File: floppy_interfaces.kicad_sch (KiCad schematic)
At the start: 23 parts, among them J13 Conn_01x04_Male, J14 Conn_02x17_Odd_Even, J16 Conn_01x04_Male, J32 Mini-DIN-8-With-Shield, J6 SDF-60J for IEC 1541 serial p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, U1 74LS374, U2 74LVC374, U22 74LS06N, U3 74LVC374, U4 74LS374

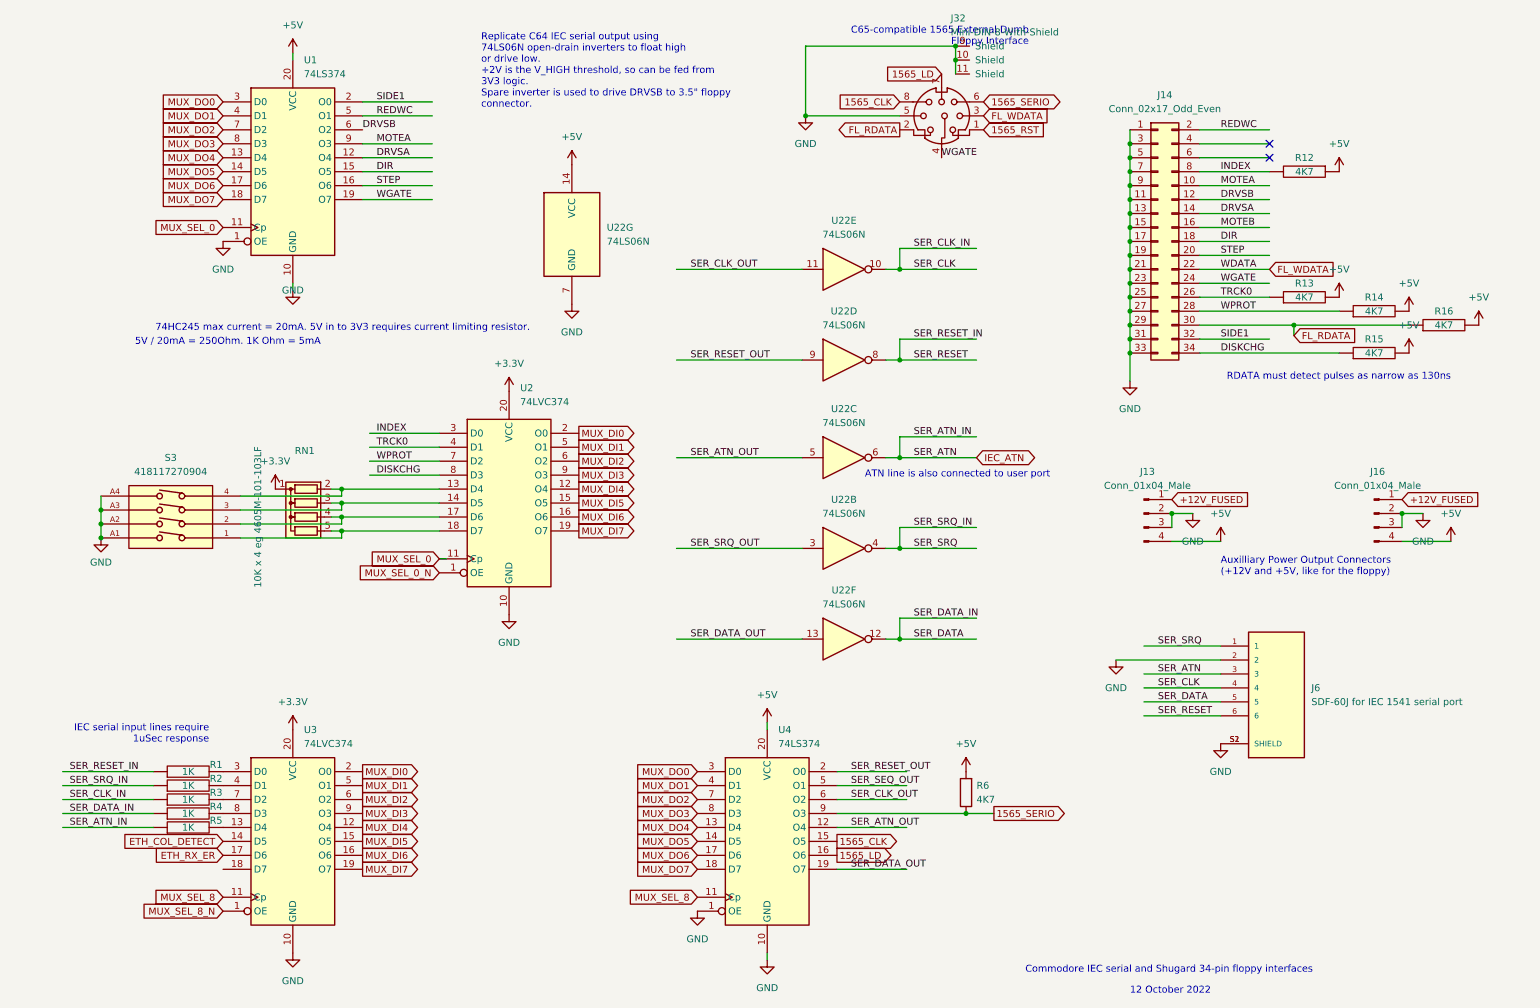
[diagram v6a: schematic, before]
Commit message: rework user port
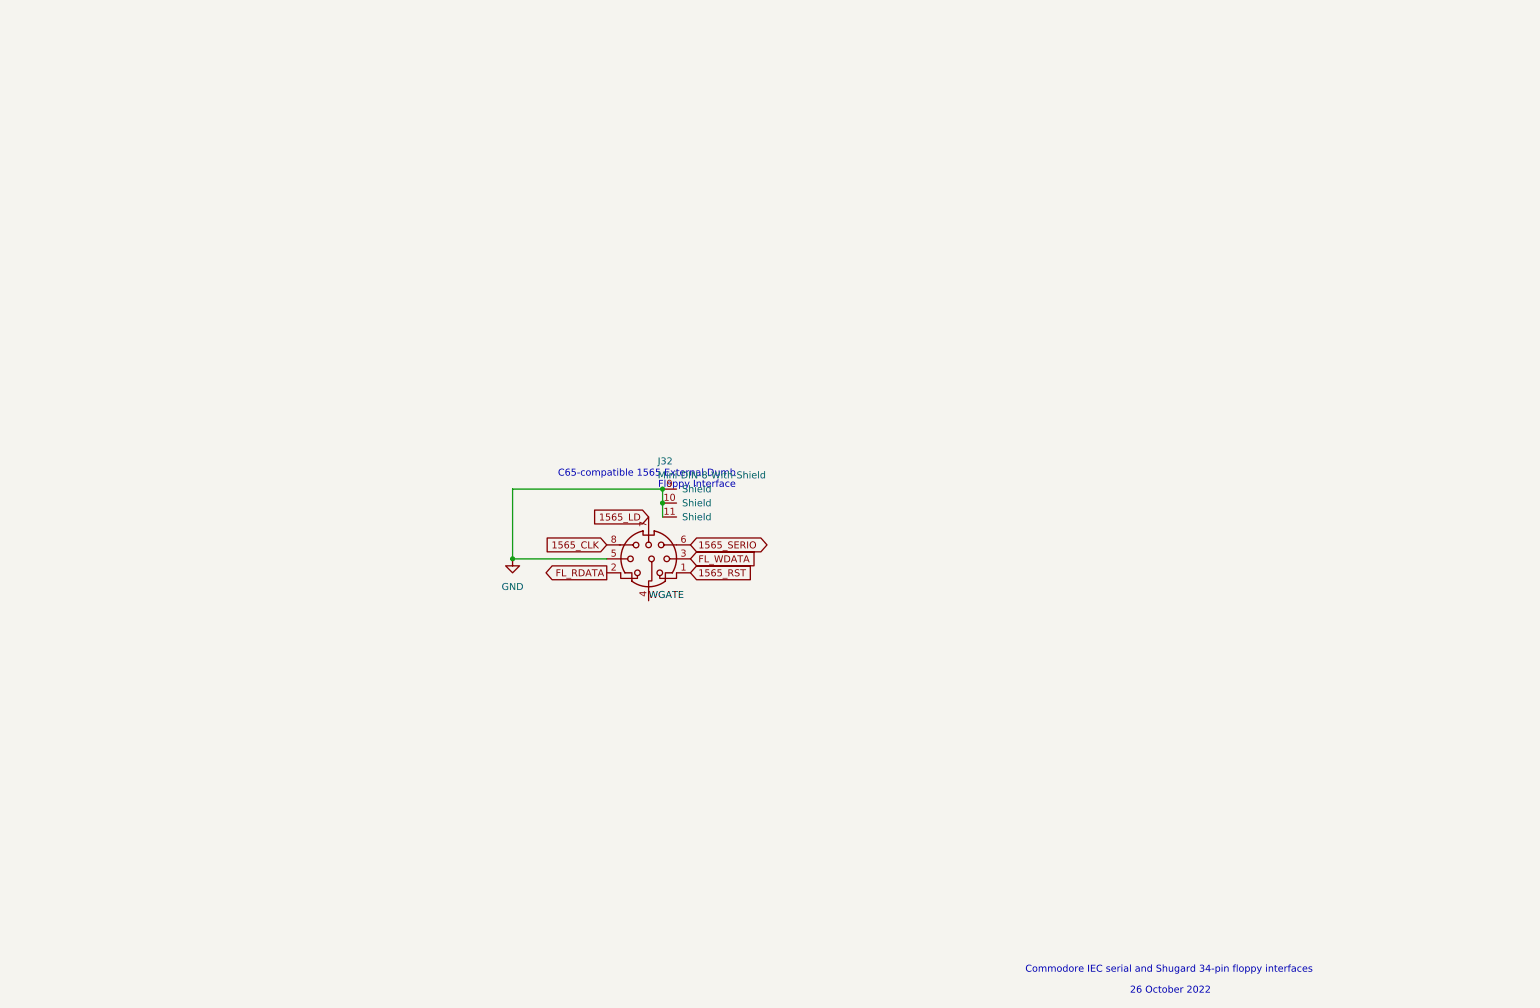
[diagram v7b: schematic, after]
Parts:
- removed J13, J16: Conn_01x04_Male, Connector_PinHeader_2.54mm:PinHeader_1x04_P2.54mm_Vertical, symbol Connector:Conn_01x04_Male
- removed J14: Conn_02x17_Odd_Even, Connector_PinHeader_2.54mm:PinHeader_2x17_P2.54mm_Vertical, symbol Connector_Generic:Conn_02x17_Odd_Even
- removed J6: SDF-60J for IEC 1541 serial port, snapeda:CUI_SDF-60J, symbol snapeda:SDF-60J
- removed R1, R2, R3, R4, R5: 1K, snapeda:Labeled Resistor, symbol pspice:R
- removed R12, R13, R14, R15, R16: 4K7, snapeda:Labeled Resistor, symbol pspice:R
- removed R6: 4K7, snapeda:Labeled Resistor, symbol Device:R
- removed RN1: 10K x 4 eg 4605M-101-103LF, Resistor_THT:R_Array_SIP5, symbol Device:R_Network04
- removed S3: 418117270904, 418117270904, symbol 00Project-DIP-SW-4:418117270904
- removed U1, U4: 74LS374, snapeda:DIP-20_LS_Family, symbol 74xx:74LS374
- removed U2, U3: 74LVC374, snapeda:DIP-20_LVC_Family, symbol 74xx:74HC374
- removed U22: 74LS06N, snapeda:DIP-14_74LS06, symbol 74xx:74LS06N
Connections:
- no-connect marks 2 -> 0
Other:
- note added: "26 October 2022"
- note removed: "12 October 2022"
- note removed: "5V / 20mA = 250Ohm. 1K Ohm = 5mA"
- note removed: "74HC245 max current = 20mA. 5V in to 3V3 requires current limiting resistor."
- note removed: "ATN line is also connected to user port"
- note removed: "Auxilliary Power Output Connectors (+12V and +5V, like for the floppy)"
- note removed: "IEC serial input lines require 1uSec response"
- note removed: "RDATA must detect pulses as narrow as 130ns"
- note removed: "Replicate C64 IEC serial output using 74LS06N open-drain inverters to float high or drive low. +2V is the V_HIGH threshold, so can be fed from 3V3 logic. Spare inverter is used to drive DRVSB to 3.5" floppy connector."
- moved on the sheet: J32
